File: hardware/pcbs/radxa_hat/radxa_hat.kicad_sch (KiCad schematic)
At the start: 6 parts, among them J1 Conn_02x20_Odd_Even

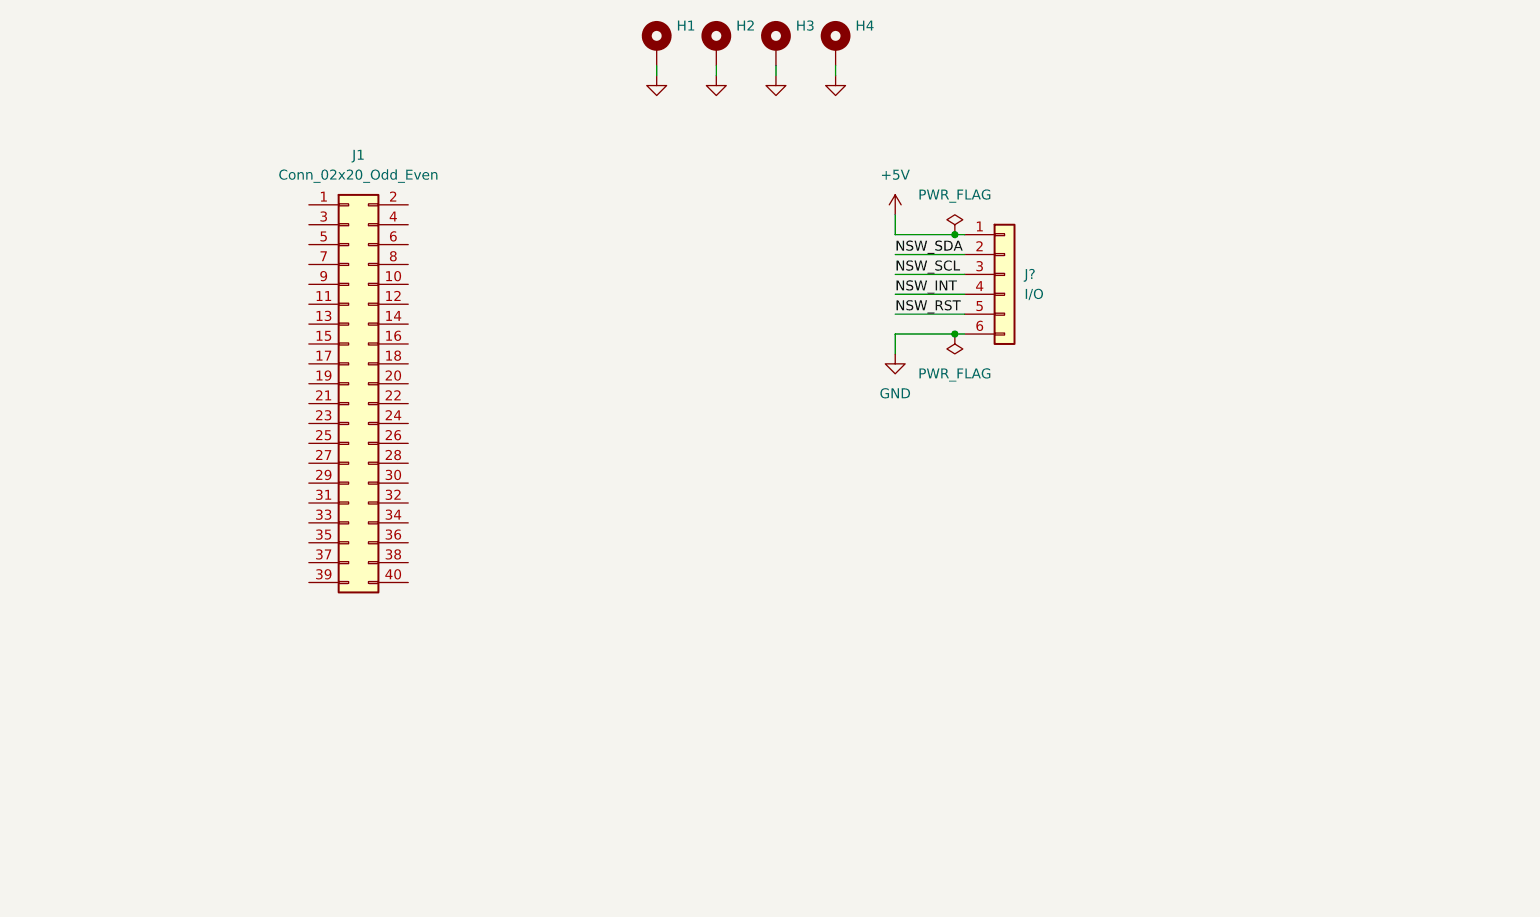
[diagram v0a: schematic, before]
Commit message: hat_pcbs: add radxa hat
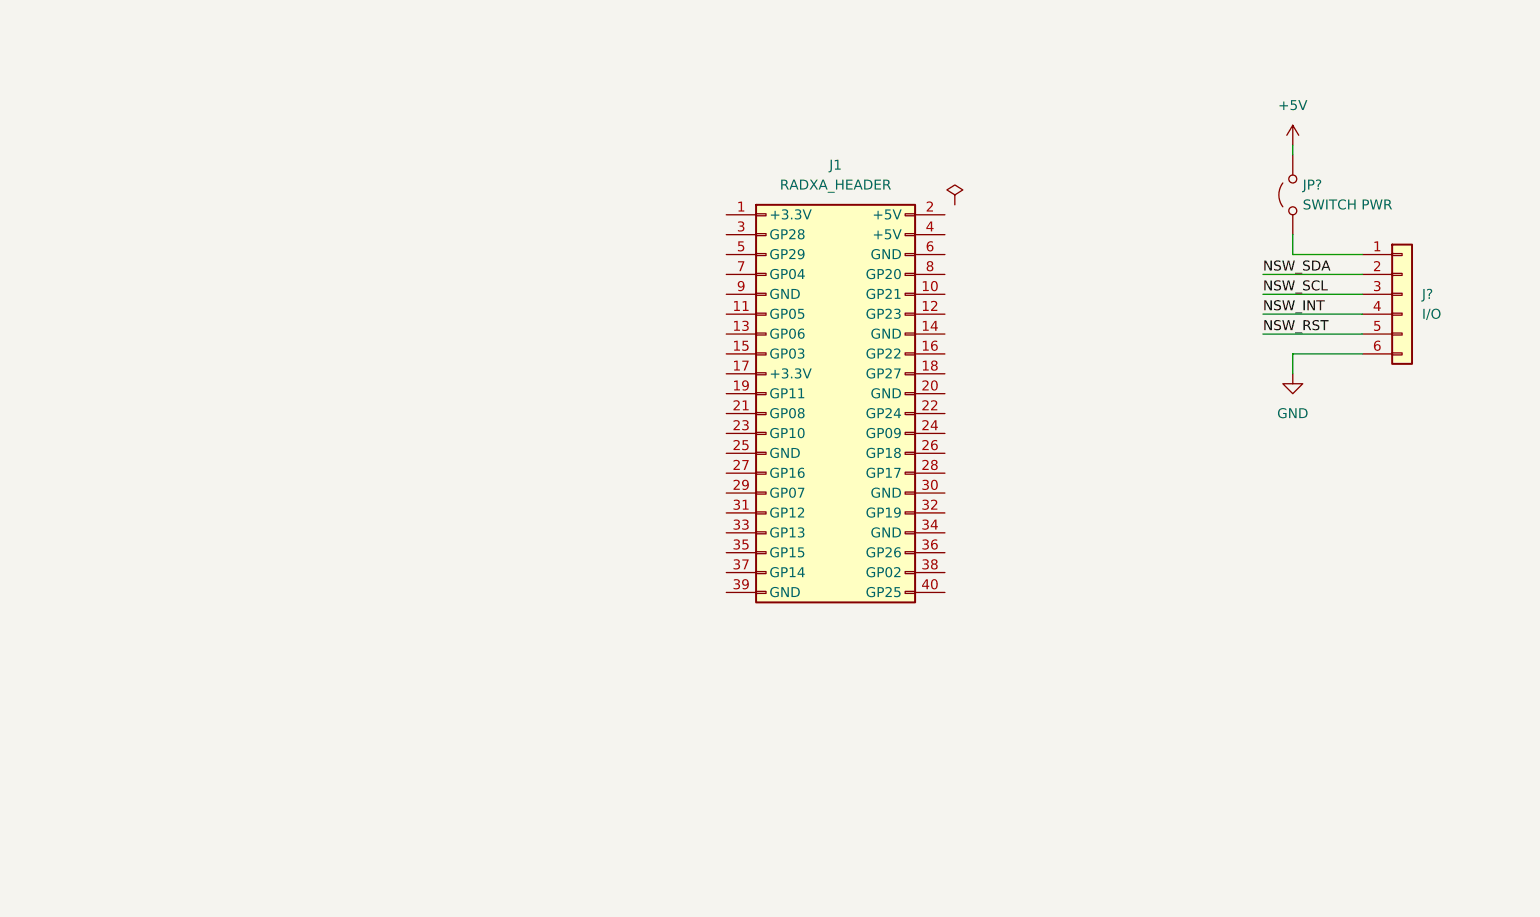
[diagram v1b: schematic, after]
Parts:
- removed H1, H2, H3, H4: MountingHole_Pad, MountingHole:MountingHole_2.2mm_M2_ISO7380_Pad, symbol Mechanical:MountingHole_Pad
- removed J1: Conn_02x20_Odd_Even, Connector_PinHeader_2.54mm:PinHeader_2x20_P2.54mm_Vertical, symbol Connector_Generic:Conn_02x20_Odd_Even
- removed J?: I/O, Library:mta100_01x6_P2.54_647050-6, symbol Connector_Generic:Conn_01x06
- added J1: RADXA_HEADER, Connector_PinSocket_2.54mm:PinSocket_2x20_P2.54mm_Vertical, symbol conn:radxa_header
- added J?: I/O, Library:mta100_01x6_P2.54_647050-6, symbol Connector_Generic:Conn_01x06
- added JP?: SWITCH PWR, symbol Jumper:Jumper_2_Open
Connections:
- net +5V: now also JP?.2 (B)
- net GND: now also J?.6 (Pin_6)
- net NSW_INT: now also J?.4 (Pin_4)
- net NSW_RST: now also J?.5 (Pin_5)
- net NSW_SCL: now also J?.3 (Pin_3)
- net NSW_SDA: now also J?.2 (Pin_2)
- new net: J?.1 (Pin_1), JP?.1 (A)

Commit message: hats_pcbs: add some connectors
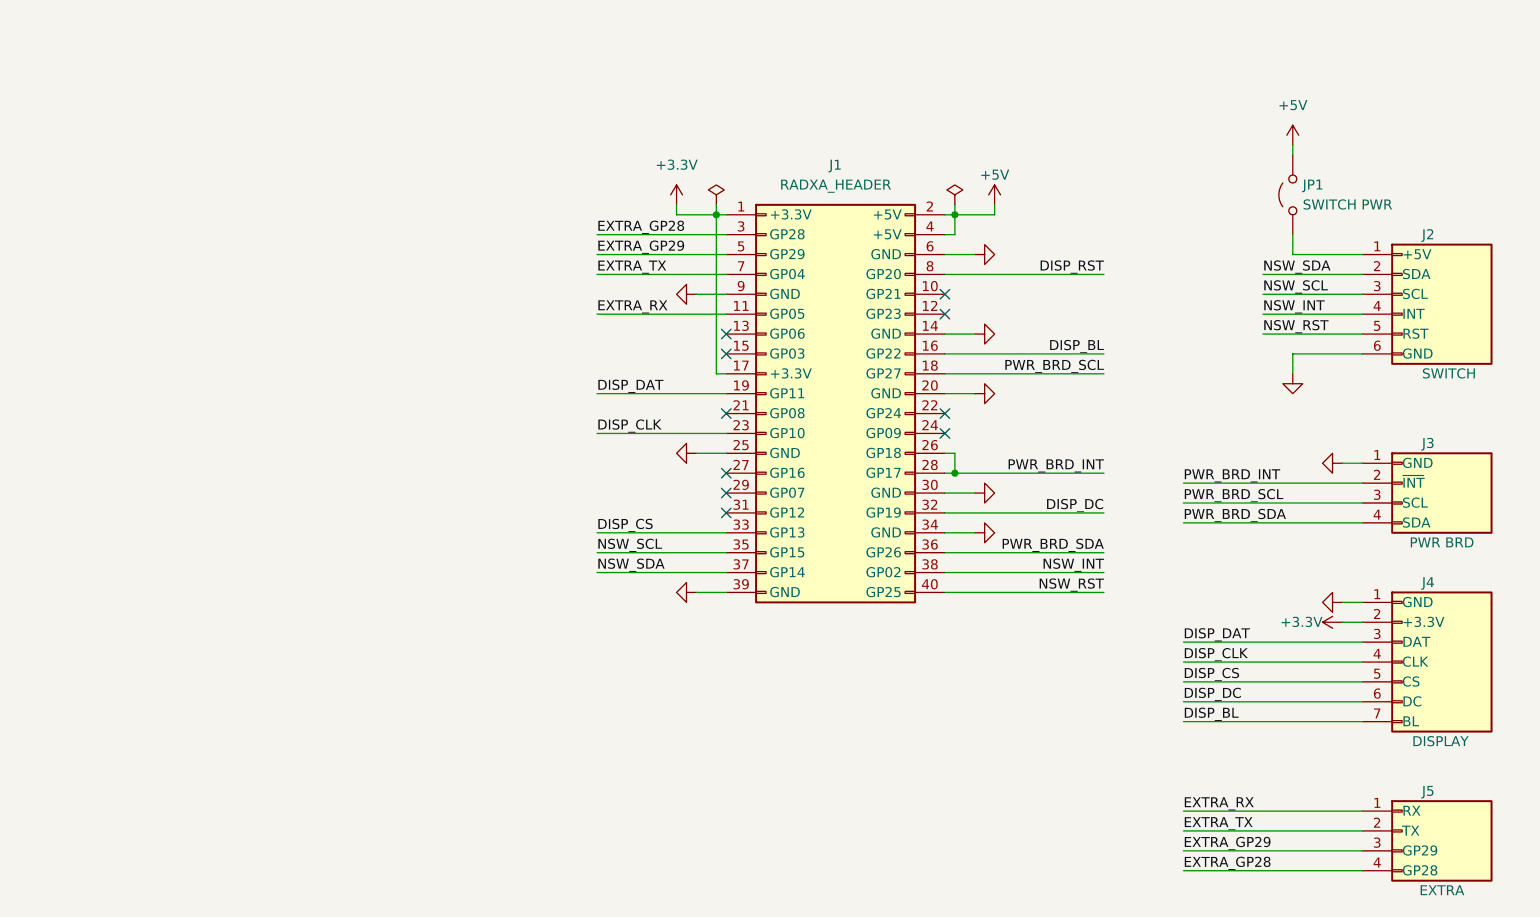
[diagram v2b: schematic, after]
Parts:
- removed J?: I/O, Library:mta100_01x6_P2.54_647050-6, symbol Connector_Generic:Conn_01x06
- added J2: Header_01x06, Connector_MTA-100:mta100_01x6_P2.54_640455-6, symbol conn:Conn_01x06
- added J3, J5: Header_01x04, Connector_MTA-100:mta100_01x4_P2.54_640455-4, symbol conn:Conn_01x04
- added J4: Header_01x06, Connector_MTA-100:mta100_01x7_P2.54_640455-7, symbol conn:Conn_01x07
- JP1: renamed from JP?; footprint (none) -> Connector_PinHeader_2.54mm:PinHeader_1x02_P2.54mm_Vertical; Part Jumper_2 -> Header_Angled_2
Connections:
- net +5V: now also J1.2 (+5V), J1.4 (+5V)
- net GND: now also J1.14 (GND), J1.20 (GND), J1.25 (GND), J1.30 (GND), J1.34 (GND), J1.39 (GND), J1.6 (GND), J1.9 (GND), J2.6 (Pin_6), J3.1 (Pin_1), J4.1 (Pin_1)
- net NSW_INT: now also J1.38 (GP02), J2.4 (Pin_4)
- net NSW_RST: now also J1.40 (GP25), J2.5 (Pin_5)
- net NSW_SCL: now also J1.35 (GP15), J2.3 (Pin_3)
- net NSW_SDA: now also J1.37 (GP14), J2.2 (Pin_2)
- net at JP1.1 (A): now also J2.1 (Pin_1)
- net +3.3V: now reaches J1.1 (+3.3V)
- net +3.3V: now also J1.17 (+3.3V), J4.2 (Pin_2)
- net EXTRA_RX: now reaches J1.11 (GP05)
- net EXTRA_RX: now also J5.1 (Pin_1)
- net DISP_BL: now reaches J1.16 (GP22)
- net DISP_BL: now also J4.7 (Pin_7)
- net PWR_BRD_SCL: now reaches J1.18 (GP27)
- net PWR_BRD_SCL: now also J3.3 (Pin_3)
- net DISP_DAT: now reaches J1.19 (GP11)
- net DISP_DAT: now also J4.3 (Pin_3)
- net DISP_CLK: now reaches J1.23 (GP10)
- net DISP_CLK: now also J4.4 (Pin_4)
- net PWR_BRD_INT: now reaches J1.26 (GP18)
- net PWR_BRD_INT: now also J1.28 (GP17), J3.2 (Pin_2)
- net EXTRA_GP28: now reaches J1.3 (GP28)
- net EXTRA_GP28: now also J5.4 (Pin_4)
- net DISP_DC: now reaches J1.32 (GP19)
- net DISP_DC: now also J4.6 (Pin_6)
- net DISP_CS: now reaches J1.33 (GP13)
- net DISP_CS: now also J4.5 (Pin_5)
- net PWR_BRD_SDA: now reaches J1.36 (GP26)
- net PWR_BRD_SDA: now also J3.4 (Pin_4)
- net EXTRA_GP29: now reaches J1.5 (GP29)
- net EXTRA_GP29: now also J5.3 (Pin_3)
- net EXTRA_TX: now reaches J1.7 (GP04)
- net EXTRA_TX: now also J5.2 (Pin_2)
- net DISP_RST: now reaches J1.8 (GP20)
- no-connect marks 0 -> 10

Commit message: hat_pcbs are almost done
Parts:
- removed J4: Header_01x06, Connector_MTA-100:mta100_01x7_P2.54_640455-7, symbol conn:Conn_01x07
- added H1, H2: MountingHole_Pad, MountingHole:MountingHole_3.2mm_M3_DIN965_Pad, symbol Mechanical:MountingHole_Pad
- added J4: Header_01x08, Connector_MTA-100:mta100_01x8_P2.54_640455-8, symbol conn:Conn_01x08
- J2: Purpose Pin1 +5V -> GND; Purpose Pin2 SCL -> INT; Purpose Pin3 SDA -> RST; Purpose Pin4 INT -> SCL; Purpose Pin5 RST -> SDA; Purpose Pin6 GND -> +5V
- J3: Purpose Pin1 GND -> SDA; Purpose Pin2 ~{INT} -> SCL; Purpose Pin3 SCL -> INT; Purpose Pin4 SDA -> GND
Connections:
- net +3.3V: now also J4.2 (Pin_2)
- net DISP_BL: now also J4.7 (Pin_7)
- net DISP_CLK: now also J4.5 (Pin_5)
- net DISP_CS: now also J4.3 (Pin_3)
- net DISP_DAT: now also J4.6 (Pin_6)
- net DISP_DC: now also J4.4 (Pin_4)
- net DISP_RST: now also J4.8 (Pin_8)
- net GND: now also J2.1 (Pin_1), J3.4 (Pin_4), H1.1, H2.1, J4.1 (Pin_1); no longer J2.6 (Pin_6), J3.1 (Pin_1)
- net NSW_INT: now also J2.3 (Pin_3); no longer J2.4 (Pin_4)
- net NSW_RST: now also J2.2 (Pin_2); no longer J2.5 (Pin_5)
- net NSW_SCL: now also J2.4 (Pin_4); no longer J2.3 (Pin_3)
- net NSW_SDA: now also J2.5 (Pin_5); no longer J2.2 (Pin_2)
- net PWR_BRD_INT: now also J3.3 (Pin_3); no longer J3.2 (Pin_2)
- net PWR_BRD_SCL: now also J3.2 (Pin_2); no longer J3.3 (Pin_3)
- net PWR_BRD_SDA: now also J3.1 (Pin_1); no longer J3.4 (Pin_4)
- net at JP1.1 (A): now also J2.6 (Pin_6); no longer J2.1 (Pin_1)

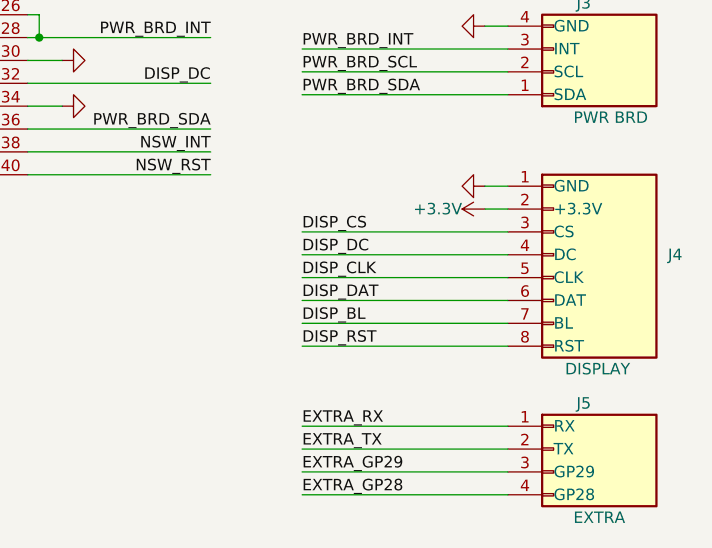
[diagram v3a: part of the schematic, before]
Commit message: hat_pcbs: add some resistors
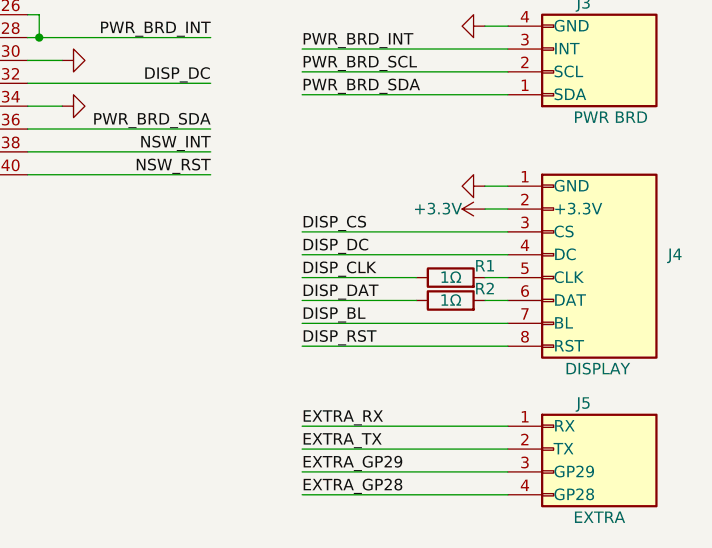
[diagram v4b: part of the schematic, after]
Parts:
- added R1, R2: 1Ω, Resistor_SMD:R_0805_2012Metric, symbol Device:R
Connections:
- net DISP_CLK: now also R1.1; no longer J4.5 (Pin_5)
- net DISP_DAT: now also R2.1; no longer J4.6 (Pin_6)
- new net: J4.5 (Pin_5), R1.2
- new net: J4.6 (Pin_6), R2.2
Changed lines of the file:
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@@
+	(wire
+		(pts
+			(xy 182.88 116.84) (xy 195.58 116.84)
+		)
+		(stroke
+			(width 0)
+			(type default)
+		)
+	)
 	(wire
 		(pts
@@
 	(wire
 		(pts
+			(xy 182.88 114.3) (xy 195.58 114.3)
+		)
+		(stroke
+			(width 0)
+			(type default)
+		)
+	)
+	(wire
+		(pts
 			(xy 196.85 59.69) (xy 205.74 59.69)
 		)
@@
 	(wire
 		(pts
-			(xy 182.88 114.3) (xy 205.74 114.3)
-		)
-		(stroke
-			(width 0)
-			(type default)
-		)
-	)
-	(wire
-		(pts
-			(xy 182.88 116.84) (xy 205.74 116.84)
-		)
-		(stroke
-			(width 0)
-			(type default)
-		)
-	)
-	(wire
-		(pts
 			(xy 196.85 57.15) (xy 196.85 59.69)
 		)
@@
 	(wire
 		(pts
+			(xy 203.2 116.84) (xy 205.74 116.84)
+		)
+		(stroke
+			(width 0)
+			(type default)
+		)
+	)
+	(wire
+		(pts
 			(xy 123.19 102.87) (xy 123.19 105.41)
+		)
+		(stroke
+			(width 0)
+			(type default)
+		)
+	)
+	(wire
+		(pts
+			(xy 203.2 114.3) (xy 205.74 114.3)
 		)
 		(stroke
@@
 	)
 	(symbol
+		(lib_id "Device:R")
+		(at 199.39 114.3 90)
+		(unit 1)
+		(exclude_from_sim no)
+		(in_bom yes)
+		(on_board yes)
+		(dnp no)
+		(property "Reference" "R1"
+			(at 203.2 113.03 90)
+			(effects
+				(font
+					(size 1.27 1.27)
+				)
+			)
+		)
+		(property "Value" "1Ω"
+			(at 199.39 114.3 90)
+			(effects
+				(font
+					(size 1.27 1.27)
+				)
+			)
+		)
+		(property "Footprint" "Resistor_SMD:R_0805_2012Metric"
+			(at 199.39 116.078 90)
+			(effects
+				(font
+					(size 1.27 1.27)
+				)
+				(hide yes)
+			)
+		)
+		(property "Datasheet" "~"
+			(at 199.39 114.3 0)
+			(effects
+				(font
+					(size 1.27 1.27)
+				)
+				(hide yes)
+			)
+		)
+		(property "Description" "Resistor"
+			(at 199.39 114.3 0)
+			(effects
+				(font
+					(size 1.27 1.27)
+				)
+				(hide yes)
+			)
+		)
+		(pin "2"
+		)
+		(pin "1"
+		)
+		(instances
+			(project ""
+				(path "/9fb68e6f-3a80-4125-99a9-9e938d51af87"
+					(reference "R1")
+					(unit 1)
+				)
+			)
+		)
+	)
+	(symbol
 		(lib_id "power:+3.3V")
 		(at 203.2 106.68 90)
@@
 					(unit 1)
 				)
+			)
+		)
+	)
+	(symbol
+		(lib_id "Device:R")
+		(at 199.39 116.84 90)
+		(unit 1)
+		(exclude_from_sim no)
+		(in_bom yes)
+		(on_board yes)
+		(dnp no)
+		(property "Reference" "R2"
+			(at 203.2 115.57 90)
+			(effects
+				(font
+					(size 1.27 1.27)
+				)
+			)
+		)
+		(property "Value" "1Ω"
+			(at 199.39 116.84 90)
+			(effects
+				(font
+					(size 1.27 1.27)
+				)
+			)
+		)
+		(property "Footprint" "Resistor_SMD:R_0805_2012Metric"
+			(at 199.39 118.618 90)
+			(effects
+				(font
+					(size 1.27 1.27)
+				)
+				(hide yes)
+			)
+		)
+		(property "Datasheet" "~"
+			(at 199.39 116.84 0)
+			(effects
+				(font
+					(size 1.27 1.27)
+				)
+				(hide yes)
+			)
+		)
+		(property "Description" "Resistor"
+			(at 199.39 116.84 0)
+			(effects
+				(font
+					(size 1.27 1.27)
+				)
+				(hide yes)
+			)
+		)
+		(pin "2"
+		)
+		(pin "1"
+		)
+		(instances
+			(project "radxa_hat"
+				(path "/9fb68e6f-3a80-4125-99a9-9e938d51af87"
+					(reference "R2")
+					(unit 1)
+				)

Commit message: pcbs: update purchase info
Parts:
- J1: Part (none) -> CB91402V100; Shop (none) -> https://store.comet.bg/Catalogue/Product/10029/
- J2: Part (none) -> 640456-6; Shop (none) -> https://eu.mouser.com/ProductDetail/TE-Connectivity-AMP/640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
- J4: Part (none) -> 640456-8; Shop (none) -> https://eu.mouser.com/ProductDetail/TE-Connectivity-AMP/640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
- R1, R2: Part (none) -> R 1Ω 125mW 1% 0805; Shop (none) -> https://store.comet.bg/Catalogue/Product/9926/
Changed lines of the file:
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@@
 		)
 		(instances
-			(project ""
+			(project "radxa_hat"
 				(path "/9fb68e6f-3a80-4125-99a9-9e938d51af87"
 					(reference "#PWR012")
@@
 		)
 		(instances
-			(project ""
+			(project "radxa_hat"
 				(path "/9fb68e6f-3a80-4125-99a9-9e938d51af87"
 					(reference "#PWR03")
@@
 			)
 		)
+		(property "Part" "640456-6"
+			(at 210.82 69.85 0)
+			(effects
+				(font
+					(size 1.27 1.27)
+				)
+				(hide yes)
+			)
+		)
+		(property "Shop" "https://eu.mouser.com/ProductDetail/TE-Connectivity-AMP/640456-6?qs=%2F35zJ5USjomb%252BGgX%252BBnrrQ%3D%3D"
+			(at 210.82 69.85 0)
+			(effects
+				(font
+					(size 1.27 1.27)
+				)
+				(hide yes)
+			)
+		)
 		(pin "3"
 		)
@@
 		)
 		(instances
-			(project ""
+			(project "radxa_hat"
 				(path "/9fb68e6f-3a80-4125-99a9-9e938d51af87"
 					(reference "J2")
@@
 			)
 		)
+		(property "Part" "R 1Ω 125mW 1% 0805"
+			(at 199.39 114.3 0)
+			(effects
+				(font
+					(size 1.27 1.27)
+				)
+				(hide yes)
+			)
+		)
+		(property "Shop" "https://store.comet.bg/Catalogue/Product/9926/"
+			(at 199.39 114.3 0)
+			(effects
+				(font
+					(size 1.27 1.27)
+				)
+				(hide yes)
+			)
+		)
 		(pin "2"
 		)
@@
 		)
 		(instances
-			(project ""
+			(project "radxa_hat"
 				(path "/9fb68e6f-3a80-4125-99a9-9e938d51af87"
 					(reference "R1")
@@
 			)
 		)
+		(property "Part" "CB91402V100"
+			(at 138.43 77.47 0)
+			(effects
+				(font
+					(size 1.27 1.27)
+				)
+				(hide yes)
+			)
+		)
+		(property "Shop" "https://store.comet.bg/Catalogue/Product/10029/"
+			(at 138.43 77.47 0)
+			(effects
+				(font
+					(size 1.27 1.27)
+				)
+				(hide yes)
+			)
+		)
 		(pin "38"
 		)
@@
 			)
 		)
+		(property "Part" "640456-8"
+			(at 210.82 106.68 0)
+			(effects
+				(font
+					(size 1.27 1.27)
+				)
+				(hide yes)
+			)
+		)
+		(property "Shop" "https://eu.mouser.com/ProductDetail/TE-Connectivity-AMP/640456-8?qs=%2F35zJ5USjomho1287DA4QA%3D%3D"
+			(at 210.82 106.68 0)
+			(effects
+				(font
+					(size 1.27 1.27)
+				)
+				(hide yes)
+			)
+		)
 		(pin "2"
 		)
@@
 		)
 		(instances
-			(project ""
+			(project "radxa_hat"
 				(path "/9fb68e6f-3a80-4125-99a9-9e938d51af87"
 					(reference "J4")
@@
 			(at 199.39 116.84 0)
 			(effects
+				(font
+					(size 1.27 1.27)
+				)
+				(hide yes)
+			)
+		)
+		(property "Part" "R 1Ω 125mW 1% 0805"
+			(at 199.39 116.84 0)
+			(effects
+				(font
+					(size 1.27 1.27)
+				)
+				(hide yes)
+			)
+		)
+		(property "Shop" "https://store.comet.bg/Catalogue/Product/9926/"
+			(at 199.39 116.84 0)
+			(effects

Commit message: boards: update boms again
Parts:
- J1: Part CB91402V100 -> HeaderSocket_2x20
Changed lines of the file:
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@@
 			)
 		)
-		(property "Part" "CB91402V100"
+		(property "Part" "HeaderSocket_2x20"
 			(at 138.43 77.47 0)
 			(effects
